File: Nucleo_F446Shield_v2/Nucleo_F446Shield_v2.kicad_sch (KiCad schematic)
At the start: 46 parts, among them J1 Barrel_Jack, J19 I2C3, J2 Conn_02x13_Odd_Even, J20 UART4, J21 xt60 male, J3 CAN1, J4 CAN2, SW1 SW1, SW11 DIP1, SW2 SW2, SW3 SW3, U1 NUCLEO-F446RE, U2 MP1584, U3 TJA1050, U4 TJA1050

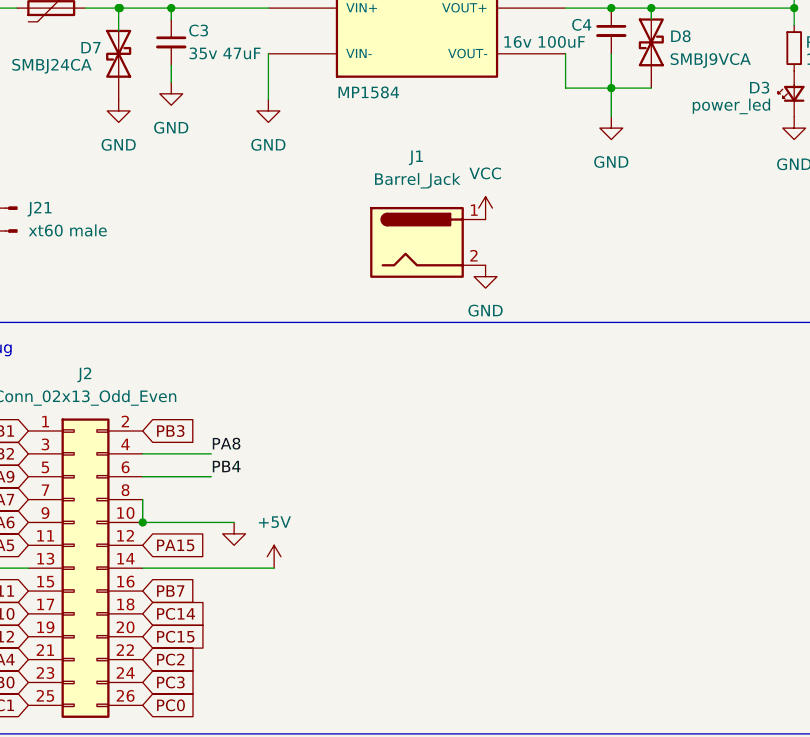
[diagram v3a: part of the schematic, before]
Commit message: power connector added
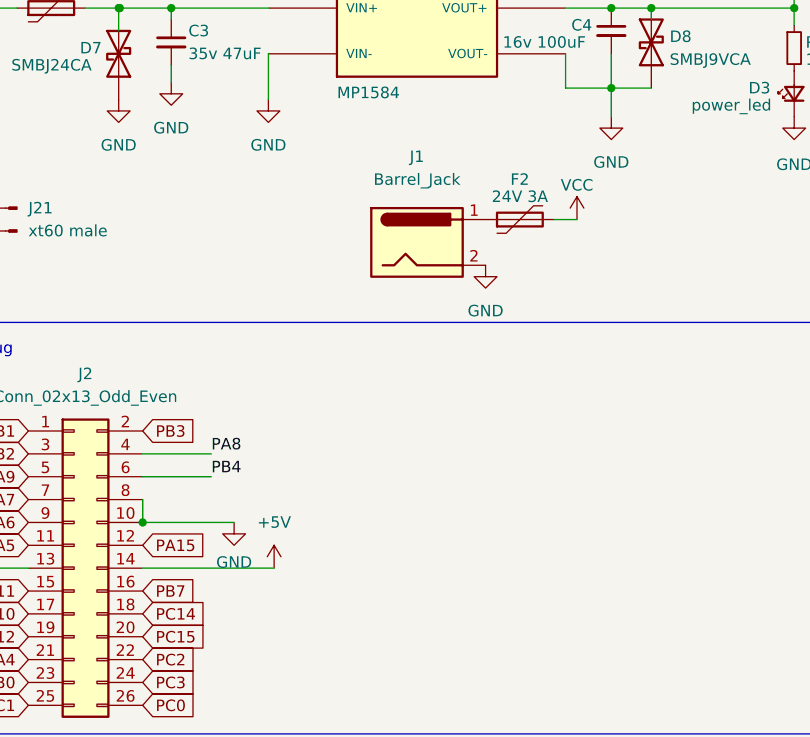
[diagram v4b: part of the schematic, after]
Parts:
- added F2: 24V 3A, Fuse:Fuse_1812_4532Metric_Pad1.30x3.40mm_HandSolder, symbol Device:Polyfuse
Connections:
- net VCC: now also F2.2; no longer J1.1
- new net: F2.1, J1.1
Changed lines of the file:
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@@
+    (stroke (width 0) (type default) (color 0 0 0 0))
+  )
+  (wire (pts (xy 254 45.72) (xy 251.46 45.72))
     (stroke (width 0) (type default) (color 0 0 0 0))
   )
@@
     (pin "2")
   )
+  (symbol (lib_id "power:VCC") (at 254 45.72 0) (unit 1)
+    (in_bom yes) (on_board yes)
+    (property "Reference" "#PWR0103" (id 0) (at 254 49.53 0)
+      (effects (font (size 1.27 1.27)) hide)
+    )
+    (property "Value" "VCC" (id 1) (at 254 41.91 0))
+    (property "Footprint" "" (id 2) (at 254 45.72 0)
+      (effects (font (size 1.27 1.27)) hide)
+    )
+    (property "Datasheet" "" (id 3) (at 254 45.72 0)
+      (effects (font (size 1.27 1.27)) hide)
+    )
+    (pin "1")
+  )
   (symbol (lib_id "power:GND") (at 203.073 32.385 0) (unit 1)
     (in_bom yes) (on_board yes) (fields_autoplaced)
@@
       (effects (font (size 1.27 1.27)) hide)
     )
-    (property "Value" "" (id 1) (at 215.9 83.82 0))
+    (property "Value" "GND" (id 1) (at 215.9 83.82 0))
     (property "Footprint" "" (id 2) (at 215.9 79.375 0)
       (effects (font (size 1.27 1.27)) hide)
@@
     )
     (pin "1")
+  )
+  (symbol (lib_id "Device:Polyfuse") (at 247.65 45.72 90) (unit 1)
+    (in_bom yes) (on_board yes)
+    (property "Reference" "F2" (id 0) (at 247.65 41.275 90))
+    (property "Value" "24V 3A" (id 1) (at 247.65 43.18 90))
+    (property "Footprint" "Fuse:Fuse_1812_4532Metric_Pad1.30x3.40mm_HandSolder" (id 2) (at 252.73 44.45 0)
+      (effects (font (size 1.27 1.27)) (justify left) hide)
+    )
+    (property "Datasheet" "~" (id 3) (at 247.65 45.72 0)
+      (effects (font (size 1.27 1.27)) hide)
+    )
+    (pin "1")
+    (pin "2")
   )
   (symbol (lib_id "power:GND") (at 278.13 34.29 0) (unit 1)
@@
     (pin "2")
   )
-  (symbol (lib_id "power:VCC") (at 243.84 45.72 0) (unit 1)
-    (in_bom yes) (on_board yes) (fields_autoplaced)
-    (property "Reference" "#PWR0103" (id 0) (at 243.84 49.53 0)
-      (effects (font (size 1.27 1.27)) hide)
-    )
-    (property "Value" "VCC" (id 1) (at 243.84 40.64 0))
-    (property "Footprint" "" (id 2) (at 243.84 45.72 0)
-      (effects (font (size 1.27 1.27)) hide)
-    )
-    (property "Datasheet" "" (id 3) (at 243.84 45.72 0)
-      (effects (font (size 1.27 1.27)) hide)
-    )
-    (pin "1")
-  )
   (symbol (lib_id "Device:C_Small") (at 131.445 140.97 0) (unit 1)
     (in_bom yes) (on_board yes) (fields_autoplaced)
@@
       (reference "#PWR0102") (unit 1) (value "GND") (footprint "")
     )
-    (path "/d1cd004f-5133-4cc3-8970-e57a12bda7bd"
+    (path "/18d5a572-ddec-4d68-a4d3-adc5da42a97f"
       (reference "#PWR0103") (unit 1) (value "VCC") (footprint "")
     )
@@
       (reference "F1") (unit 1) (value "24V 3A") (footprint "Fuse:Fuse_1812_4532Metric_Pad1.30x3.40mm_HandSolder")
     )
+    (path "/99da5f8e-0bad-4c7c-b12b-47c197975e21"
+      (reference "F2") (unit 1) (value "24V 3A") (footprint "Fuse:Fuse_1812_4532Metric_Pad1.30x3.40mm_HandSolder")
+    )
     (path "/1712bce1-82b2-4061-8271-332eb75bb1a6"
